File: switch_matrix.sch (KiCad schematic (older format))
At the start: 10 parts

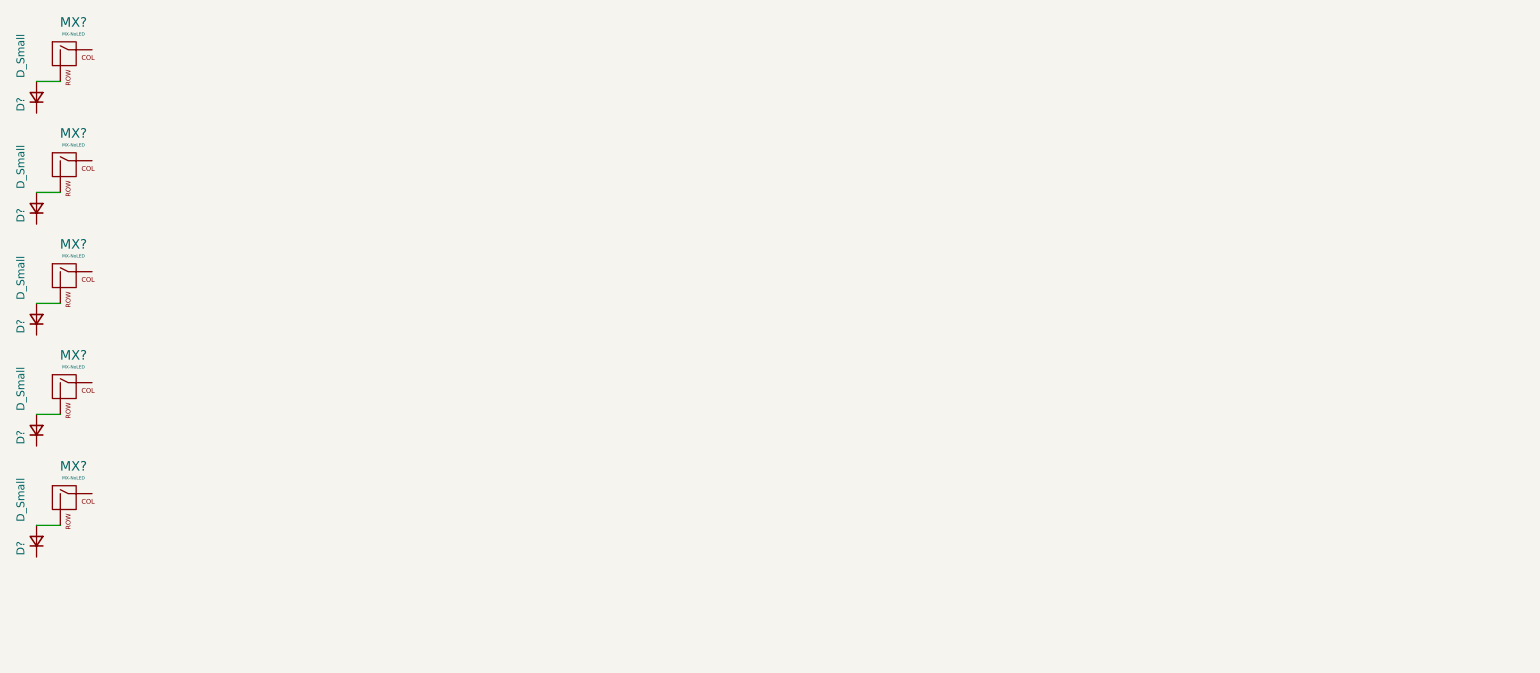
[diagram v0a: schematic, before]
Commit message: Wired switch matrix
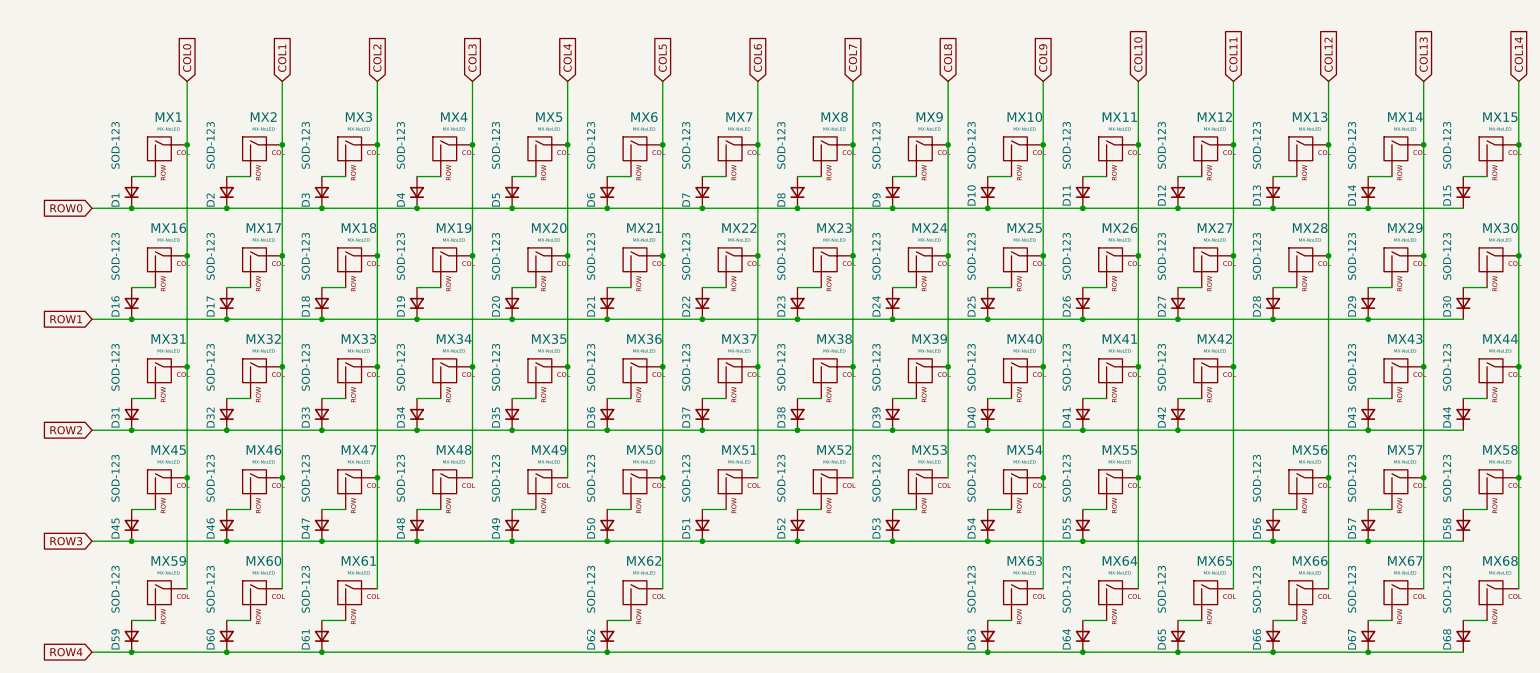
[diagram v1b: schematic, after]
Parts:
- added D10, D11, D12, D13, D14, D15, D17, D18, D19, D2, D20, D21, D22, D23, D24, D25, D26, D27, D28, D29, D3, D30, D32, D33, D34, D35, D36, D37, D38, D39, D4, D40, D41, D42, D43, D44, D46, D47, D48, D49, D5, D50, D51, D52, D53, D54, D55, D56, D57, D58, D6, D60, D61, D62, D63, D64, D65, D66, D67, D68, D7, D8, D9: SOD-123, symbol Device:D_Small
- added MX10, MX11, MX12, MX13, MX14, MX15, MX17, MX18, MX19, MX2, MX20, MX21, MX22, MX23, MX24, MX25, MX26, MX27, MX28, MX29, MX3, MX30, MX32, MX33, MX34, MX35, MX36, MX37, MX38, MX39, MX4, MX40, MX41, MX42, MX43, MX44, MX46, MX47, MX48, MX49, MX5, MX50, MX51, MX52, MX53, MX54, MX55, MX56, MX57, MX58, MX6, MX60, MX61, MX62, MX63, MX64, MX65, MX66, MX67, MX68, MX7, MX8, MX9: MX-NoLED, symbol MX_Alps_Hybrid:MX-NoLED
- D1, D16, D31, D45, D59: renamed from D?; value D_Small -> SOD-123
- gave numbers to parts that had none: 5
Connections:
- net COL0: now reaches MX1.1 (COL)
- net COL0: now also MX16.1 (COL), MX31.1 (COL), MX45.1 (COL), MX59.1 (COL)
- net ROW0: now reaches D1.1 (K)
- net ROW0: now also D10.1 (K), D11.1 (K), D12.1 (K), D13.1 (K), D14.1 (K), D15.1 (K), D2.1 (K), D3.1 (K), D4.1 (K), D5.1 (K), D6.1 (K), D7.1 (K), D8.1 (K), D9.1 (K)
- net ROW1: now reaches D16.1 (K)
- net ROW1: now also D17.1 (K), D18.1 (K), D19.1 (K), D20.1 (K), D21.1 (K), D22.1 (K), D23.1 (K), D24.1 (K), D25.1 (K), D26.1 (K), D27.1 (K), D28.1 (K), D29.1 (K), D30.1 (K)
- net ROW2: now reaches D31.1 (K)
- net ROW2: now also D32.1 (K), D33.1 (K), D34.1 (K), D35.1 (K), D36.1 (K), D37.1 (K), D38.1 (K), D39.1 (K), D40.1 (K), D41.1 (K), D42.1 (K), D43.1 (K), D44.1 (K)
- net ROW3: now reaches D45.1 (K)
- net ROW3: now also D46.1 (K), D47.1 (K), D48.1 (K), D49.1 (K), D50.1 (K), D51.1 (K), D52.1 (K), D53.1 (K), D54.1 (K), D55.1 (K), D56.1 (K), D57.1 (K), D58.1 (K)
- net ROW4: now reaches D59.1 (K)
- net ROW4: now also D60.1 (K), D61.1 (K), D62.1 (K), D63.1 (K), D64.1 (K), D65.1 (K), D66.1 (K), D67.1 (K), D68.1 (K)
- new net: D2.2 (A), MX2.2 (ROW)
- new net: D17.2 (A), MX17.2 (ROW)
- new net: D32.2 (A), MX32.2 (ROW)
- new net: D46.2 (A), MX46.2 (ROW)
- new net: D60.2 (A), MX60.2 (ROW)
- new net: D3.2 (A), MX3.2 (ROW)
- new net: D18.2 (A), MX18.2 (ROW)
- new net: D33.2 (A), MX33.2 (ROW)
- new net: D47.2 (A), MX47.2 (ROW)
- new net: D61.2 (A), MX61.2 (ROW)
- new net: D4.2 (A), MX4.2 (ROW)
- new net: D19.2 (A), MX19.2 (ROW)
- new net: D34.2 (A), MX34.2 (ROW)
- new net: D48.2 (A), MX48.2 (ROW)
- new net: D5.2 (A), MX5.2 (ROW)
- new net: D20.2 (A), MX20.2 (ROW)
- new net: D35.2 (A), MX35.2 (ROW)
- new net: D49.2 (A), MX49.2 (ROW)
- new net: D6.2 (A), MX6.2 (ROW)
- new net: D21.2 (A), MX21.2 (ROW)
- new net: D36.2 (A), MX36.2 (ROW)
- new net: D50.2 (A), MX50.2 (ROW)
- new net: D62.2 (A), MX62.2 (ROW)
- new net: D7.2 (A), MX7.2 (ROW)
- new net: D22.2 (A), MX22.2 (ROW)
- new net: D37.2 (A), MX37.2 (ROW)
- new net: D51.2 (A), MX51.2 (ROW)
- new net: D8.2 (A), MX8.2 (ROW)
- new net: D23.2 (A), MX23.2 (ROW)
- new net: D38.2 (A), MX38.2 (ROW)
- new net: D52.2 (A), MX52.2 (ROW)
- new net: D9.2 (A), MX9.2 (ROW)
- new net: D24.2 (A), MX24.2 (ROW)
- new net: D39.2 (A), MX39.2 (ROW)
- new net: D53.2 (A), MX53.2 (ROW)
- new net: D10.2 (A), MX10.2 (ROW)
- new net: D25.2 (A), MX25.2 (ROW)
- new net: D40.2 (A), MX40.2 (ROW)
- new net: D54.2 (A), MX54.2 (ROW)
- new net: D63.2 (A), MX63.2 (ROW)
- new net: D11.2 (A), MX11.2 (ROW)
- new net: D26.2 (A), MX26.2 (ROW)
- new net: D41.2 (A), MX41.2 (ROW)
- new net: D55.2 (A), MX55.2 (ROW)
- new net: D64.2 (A), MX64.2 (ROW)
- new net: D12.2 (A), MX12.2 (ROW)
- new net: D27.2 (A), MX27.2 (ROW)
- new net: D42.2 (A), MX42.2 (ROW)
- new net: D65.2 (A), MX65.2 (ROW)
- new net: D13.2 (A), MX13.2 (ROW)
- new net: D28.2 (A), MX28.2 (ROW)
- new net: D56.2 (A), MX56.2 (ROW)
- new net: D66.2 (A), MX66.2 (ROW)
- new net: D14.2 (A), MX14.2 (ROW)
- new net: D29.2 (A), MX29.2 (ROW)
- new net: D43.2 (A), MX43.2 (ROW)
- new net: D57.2 (A), MX57.2 (ROW)
- new net: D67.2 (A), MX67.2 (ROW)
- new net: D15.2 (A), MX15.2 (ROW)
- new net: D30.2 (A), MX30.2 (ROW)
- new net: D44.2 (A), MX44.2 (ROW)
- new net: D58.2 (A), MX58.2 (ROW)
- new net: D68.2 (A), MX68.2 (ROW)
- new net COL1: MX17.1 (COL), MX2.1 (COL), MX32.1 (COL), MX46.1 (COL), MX60.1 (COL)
- new net COL10: MX11.1 (COL), MX26.1 (COL), MX41.1 (COL), MX55.1 (COL), MX64.1 (COL)
- new net COL11: MX12.1 (COL), MX27.1 (COL), MX42.1 (COL), MX65.1 (COL)
- new net COL12: MX13.1 (COL), MX28.1 (COL), MX56.1 (COL), MX66.1 (COL)
- new net COL13: MX14.1 (COL), MX29.1 (COL), MX43.1 (COL), MX57.1 (COL), MX67.1 (COL)
- new net COL14: MX15.1 (COL), MX30.1 (COL), MX44.1 (COL), MX58.1 (COL), MX68.1 (COL)
- new net COL2: MX18.1 (COL), MX3.1 (COL), MX33.1 (COL), MX47.1 (COL), MX61.1 (COL)
- new net COL3: MX19.1 (COL), MX34.1 (COL), MX4.1 (COL), MX48.1 (COL)
- new net COL4: MX20.1 (COL), MX35.1 (COL), MX49.1 (COL), MX5.1 (COL)
- new net COL5: MX21.1 (COL), MX36.1 (COL), MX50.1 (COL), MX6.1 (COL), MX62.1 (COL)
- new net COL6: MX22.1 (COL), MX37.1 (COL), MX51.1 (COL), MX7.1 (COL)
- new net COL7: MX23.1 (COL), MX38.1 (COL), MX52.1 (COL), MX8.1 (COL)
- new net COL8: MX24.1 (COL), MX39.1 (COL), MX53.1 (COL), MX9.1 (COL)
- new net COL9: MX10.1 (COL), MX25.1 (COL), MX40.1 (COL), MX54.1 (COL), MX63.1 (COL)
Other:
- moved on the sheet: D1, D16, D31, D45, D59, MX1, MX16, MX31, MX45, MX59

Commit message: Assigned footprint
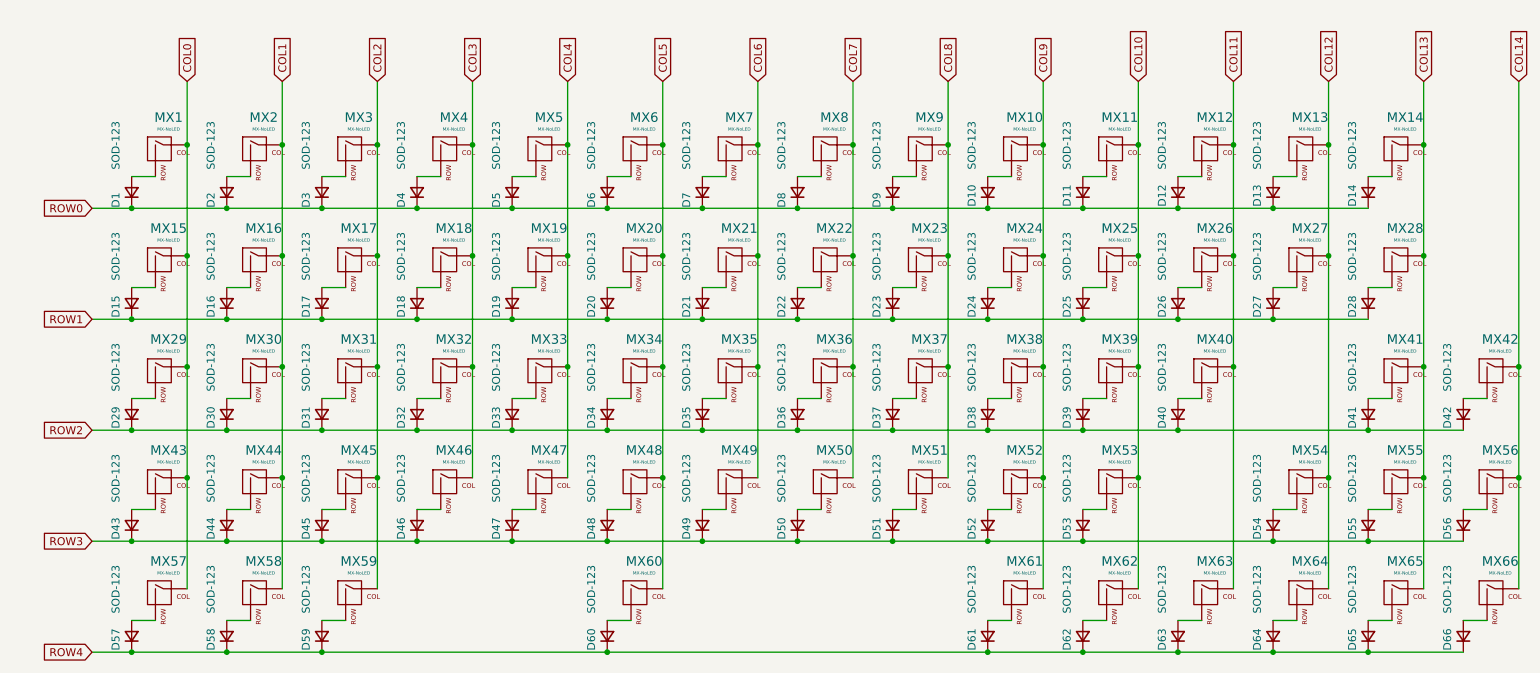
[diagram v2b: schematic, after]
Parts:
- removed D44, D58: SOD-123, symbol Device:D_Small
- removed MX44, MX58: MX-NoLED, symbol MX_Alps_Hybrid:MX-NoLED
- D1, D10, D11, D12, D13, D14, D2, D3, D4, D5, D6, D7, D8, D9: footprint (none) -> Diode_SMD:D_SOD-123
- D15: renamed from D16; footprint (none) -> Diode_SMD:D_SOD-123
- D16: renamed from D17; footprint (none) -> Diode_SMD:D_SOD-123
- D17: renamed from D18; footprint (none) -> Diode_SMD:D_SOD-123
- D18: renamed from D19; footprint (none) -> Diode_SMD:D_SOD-123
- D19: renamed from D20; footprint (none) -> Diode_SMD:D_SOD-123
- D20: renamed from D21; footprint (none) -> Diode_SMD:D_SOD-123
- D21: renamed from D22; footprint (none) -> Diode_SMD:D_SOD-123
- D22: renamed from D23; footprint (none) -> Diode_SMD:D_SOD-123
- D23: renamed from D24; footprint (none) -> Diode_SMD:D_SOD-123
- D24: renamed from D25; footprint (none) -> Diode_SMD:D_SOD-123
- D25: renamed from D26; footprint (none) -> Diode_SMD:D_SOD-123
- D26: renamed from D27; footprint (none) -> Diode_SMD:D_SOD-123
- D27: renamed from D28; footprint (none) -> Diode_SMD:D_SOD-123
- D28: renamed from D29; footprint (none) -> Diode_SMD:D_SOD-123
- D29: renamed from D31; footprint (none) -> Diode_SMD:D_SOD-123
- D30: renamed from D32; footprint (none) -> Diode_SMD:D_SOD-123
- D31: renamed from D33; footprint (none) -> Diode_SMD:D_SOD-123
- D32: renamed from D34; footprint (none) -> Diode_SMD:D_SOD-123
- D33: renamed from D35; footprint (none) -> Diode_SMD:D_SOD-123
- D34: renamed from D36; footprint (none) -> Diode_SMD:D_SOD-123
- D35: renamed from D37; footprint (none) -> Diode_SMD:D_SOD-123
- D36: renamed from D38; footprint (none) -> Diode_SMD:D_SOD-123
- D37: renamed from D39; footprint (none) -> Diode_SMD:D_SOD-123
- D38: renamed from D40; footprint (none) -> Diode_SMD:D_SOD-123
- D39: renamed from D41; footprint (none) -> Diode_SMD:D_SOD-123
- D40: renamed from D42; footprint (none) -> Diode_SMD:D_SOD-123
- D41: renamed from D43; footprint (none) -> Diode_SMD:D_SOD-123
- D42: renamed from D15; footprint (none) -> Diode_SMD:D_SOD-123
- D43: renamed from D45; footprint (none) -> Diode_SMD:D_SOD-123
- D44: renamed from D46; footprint (none) -> Diode_SMD:D_SOD-123
- D45: renamed from D47; footprint (none) -> Diode_SMD:D_SOD-123
- D46: renamed from D48; footprint (none) -> Diode_SMD:D_SOD-123
- D47: renamed from D49; footprint (none) -> Diode_SMD:D_SOD-123
- D48: renamed from D50; footprint (none) -> Diode_SMD:D_SOD-123
- D49: renamed from D51; footprint (none) -> Diode_SMD:D_SOD-123
- D50: renamed from D52; footprint (none) -> Diode_SMD:D_SOD-123
- D51: renamed from D53; footprint (none) -> Diode_SMD:D_SOD-123
- D52: renamed from D54; footprint (none) -> Diode_SMD:D_SOD-123
- D53: renamed from D55; footprint (none) -> Diode_SMD:D_SOD-123
- D54: renamed from D56; footprint (none) -> Diode_SMD:D_SOD-123
- D55: renamed from D57; footprint (none) -> Diode_SMD:D_SOD-123
- D56: renamed from D30; footprint (none) -> Diode_SMD:D_SOD-123
- D57: renamed from D59; footprint (none) -> Diode_SMD:D_SOD-123
- D58: renamed from D60; footprint (none) -> Diode_SMD:D_SOD-123
- D59: renamed from D61; footprint (none) -> Diode_SMD:D_SOD-123
- D60: renamed from D62; footprint (none) -> Diode_SMD:D_SOD-123
- D61: renamed from D63; footprint (none) -> Diode_SMD:D_SOD-123
- D62: renamed from D64; footprint (none) -> Diode_SMD:D_SOD-123
- D63: renamed from D65; footprint (none) -> Diode_SMD:D_SOD-123
- D64: renamed from D66; footprint (none) -> Diode_SMD:D_SOD-123
- D65: renamed from D67; footprint (none) -> Diode_SMD:D_SOD-123
- D66: renamed from D68; footprint (none) -> Diode_SMD:D_SOD-123
- MX1, MX10, MX11, MX12, MX13, MX2, MX3, MX4, MX5, MX6, MX7, MX8, MX9: footprint (none) -> MX_Only:MXOnly-1U-Hotswap
- MX14: footprint (none) -> MX_Only:MXOnly-2U-Hotswap
- MX15: renamed from MX16; footprint (none) -> MX_Only:MXOnly-1.5U-Hotswap
- MX16: renamed from MX17; footprint (none) -> MX_Only:MXOnly-1U-Hotswap
- MX17: renamed from MX18; footprint (none) -> MX_Only:MXOnly-1U-Hotswap
- MX18: renamed from MX19; footprint (none) -> MX_Only:MXOnly-1U-Hotswap
- MX19: renamed from MX20; footprint (none) -> MX_Only:MXOnly-1U-Hotswap
- MX20: renamed from MX21; footprint (none) -> MX_Only:MXOnly-1U-Hotswap
- MX21: renamed from MX22; footprint (none) -> MX_Only:MXOnly-1U-Hotswap
- MX22: renamed from MX23; footprint (none) -> MX_Only:MXOnly-1U-Hotswap
- MX23: renamed from MX24; footprint (none) -> MX_Only:MXOnly-1U-Hotswap
- MX24: renamed from MX25; footprint (none) -> MX_Only:MXOnly-1U-Hotswap
- MX25: renamed from MX26; footprint (none) -> MX_Only:MXOnly-1U-Hotswap
- MX26: renamed from MX27; footprint (none) -> MX_Only:MXOnly-1U-Hotswap
- MX27: renamed from MX28; footprint (none) -> MX_Only:MXOnly-1U-Hotswap
- MX28: renamed from MX29; footprint (none) -> MX_Only:MXOnly-1.5U-Hotswap
- MX29: renamed from MX31; footprint (none) -> MX_Only:MXOnly-1.75U-Hotswap
- MX30: renamed from MX32; footprint (none) -> MX_Only:MXOnly-1U-Hotswap
- MX31: renamed from MX33; footprint (none) -> MX_Only:MXOnly-1U-Hotswap
- MX32: renamed from MX34; footprint (none) -> MX_Only:MXOnly-1U-Hotswap
- MX33: renamed from MX35; footprint (none) -> MX_Only:MXOnly-1U-Hotswap
- MX34: renamed from MX36; footprint (none) -> MX_Only:MXOnly-1U-Hotswap
- MX35: renamed from MX37; footprint (none) -> MX_Only:MXOnly-1U-Hotswap
- MX36: renamed from MX38; footprint (none) -> MX_Only:MXOnly-1U-Hotswap
- MX37: renamed from MX39; footprint (none) -> MX_Only:MXOnly-1U-Hotswap
- MX38: renamed from MX40; footprint (none) -> MX_Only:MXOnly-1U-Hotswap
- MX39: renamed from MX41; footprint (none) -> MX_Only:MXOnly-1U-Hotswap
- MX40: renamed from MX42; footprint (none) -> MX_Only:MXOnly-1U-Hotswap
- MX41: renamed from MX43; footprint (none) -> MX_Only:MXOnly-2.25U-Hotswap
- MX42: renamed from MX15; footprint (none) -> MX_Only:MXOnly-1U-Hotswap
- MX43: renamed from MX45; footprint (none) -> MX_Only:MXOnly-2.25U-Hotswap
- MX44: renamed from MX46; footprint (none) -> MX_Only:MXOnly-1U-Hotswap
- MX45: renamed from MX47; footprint (none) -> MX_Only:MXOnly-1U-Hotswap
- MX46: renamed from MX48; footprint (none) -> MX_Only:MXOnly-1U-Hotswap
- MX47: renamed from MX49; footprint (none) -> MX_Only:MXOnly-1U-Hotswap
- MX48: renamed from MX50; footprint (none) -> MX_Only:MXOnly-1U-Hotswap
- MX49: renamed from MX51; footprint (none) -> MX_Only:MXOnly-1U-Hotswap
- MX50: renamed from MX52; footprint (none) -> MX_Only:MXOnly-1U-Hotswap
- MX51: renamed from MX53; footprint (none) -> MX_Only:MXOnly-1U-Hotswap
- MX52: renamed from MX54; footprint (none) -> MX_Only:MXOnly-1U-Hotswap
- MX53: renamed from MX55; footprint (none) -> MX_Only:MXOnly-1U-Hotswap
- MX54: renamed from MX56; footprint (none) -> MX_Only:MXOnly-2.25U-Hotswap
- MX55: renamed from MX57; footprint (none) -> MX_Only:MXOnly-1U-Hotswap
- MX56: renamed from MX30; footprint (none) -> MX_Only:MXOnly-1U-Hotswap
- MX57: renamed from MX59; footprint (none) -> MX_Only:MXOnly-1.25U-Hotswap
- MX58: renamed from MX60; footprint (none) -> MX_Only:MXOnly-1U-Hotswap
- MX59: renamed from MX61; footprint (none) -> MX_Only:MXOnly-1.25U-Hotswap
- MX60: renamed from MX62; footprint (none) -> MX_Only:MXOnly-6.25U-Hotswap
- MX61: renamed from MX63; footprint (none) -> MX_Only:MXOnly-1.25U-Hotswap
- MX62: renamed from MX64; footprint (none) -> MX_Only:MXOnly-1.25U-Hotswap
- MX63: renamed from MX65; footprint (none) -> MX_Only:MXOnly-1.25U-Hotswap
- MX64: renamed from MX66; footprint (none) -> MX_Only:MXOnly-1U-Hotswap
- MX65: renamed from MX67; footprint (none) -> MX_Only:MXOnly-1U-Hotswap
- MX66: renamed from MX68; footprint (none) -> MX_Only:MXOnly-1U-Hotswap
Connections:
- net ROW0: no longer D42.1 (K)
- net ROW1: no longer D56.1 (K)
- net ROW2: now also D42.1 (K)
- net ROW3: now also D56.1 (K)
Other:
- moved on the sheet: D42, D56, MX42, MX56
